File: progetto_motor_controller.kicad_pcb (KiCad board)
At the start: 4 copper layers, 66 x 75 mm, 114 parts, among them J1 USB_B_Micro, J2 Conn_01x06, J3 Conn_01x04, J4 Screw_Terminal_01x03, J5 Conn_01x05, J6 Conn_02x10_Odd_Even, J7 Conn_01x02, J8 Screw_Terminal_01x02, J9 Conn_01x03, Q1 BSC022N04LSATMA1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

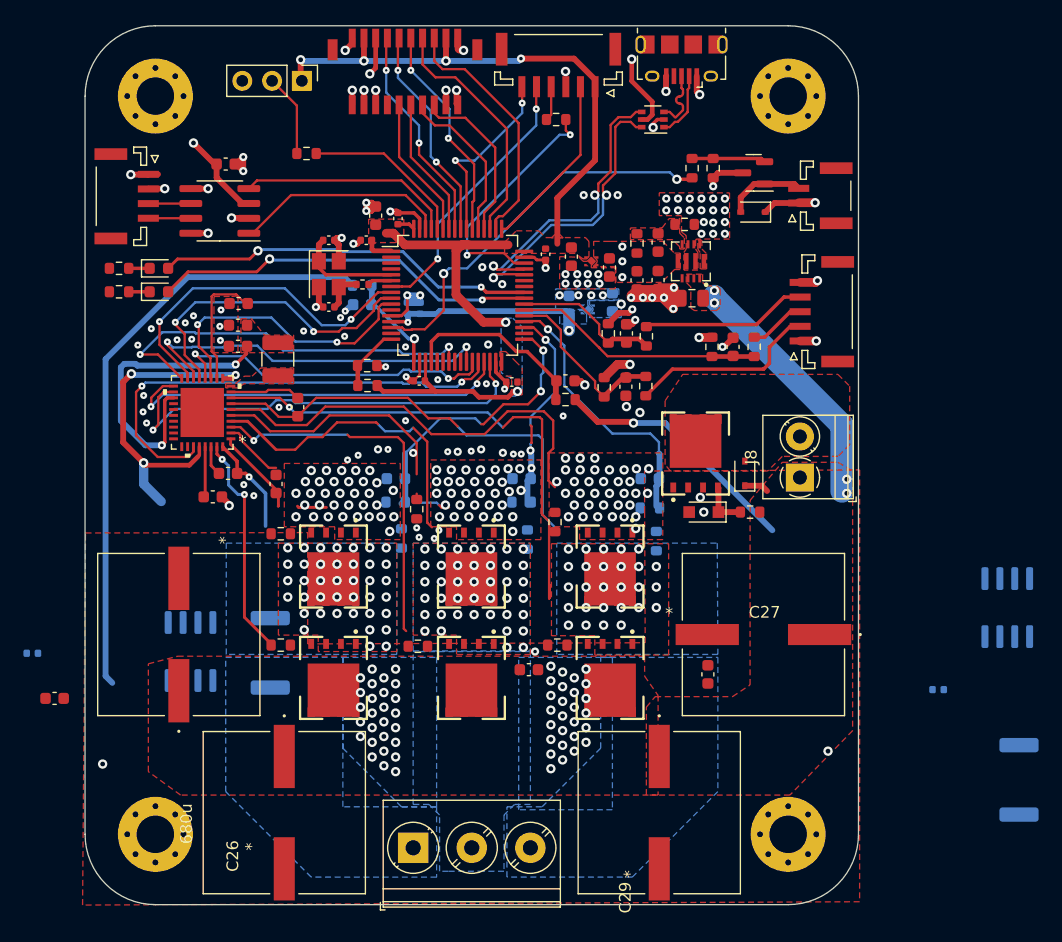
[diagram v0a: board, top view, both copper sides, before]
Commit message: added mosfet vias
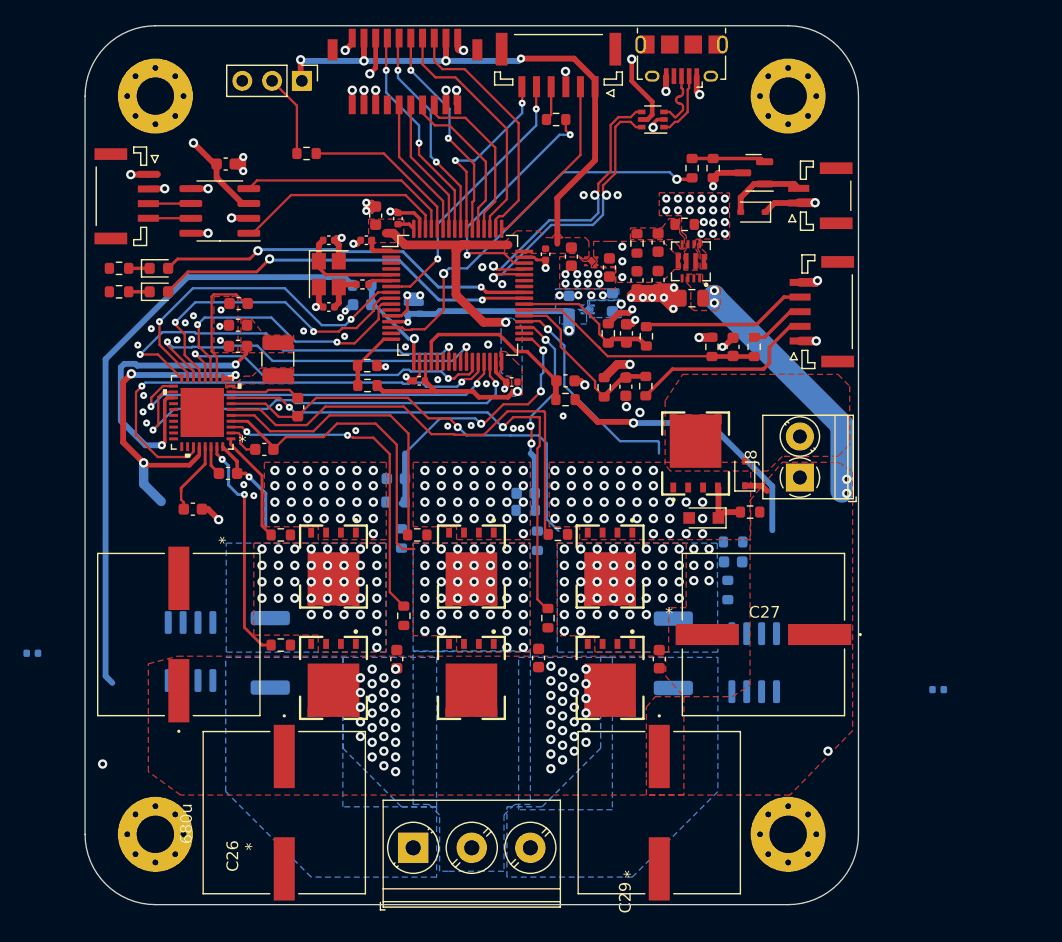
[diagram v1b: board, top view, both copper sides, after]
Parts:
- moved C20 41.4 mm to (121.7, 130.9), turned to 90 degrees
- moved R11 31.4 mm to (133.2, 130.6)
- moved U6 22.1 mm to (140.1, 131.3)
- moved C25 11.3 mm to (109.6, 131.1), turned to 90 degrees
- moved C22 10.0 mm to (138.3, 122.8), turned to 0 degrees
- moved R22 7.67 mm to (138.3, 121.0), turned to 0 degrees
- moved R19 7.39 mm to (137.8, 125.2)
- moved C23 4.35 mm to (132.0, 131.1)
- moved C14 3.11 mm to (98.3, 113.2), turned to 180 degrees
- moved R24 2.86 mm to (110.2, 127.3), turned to 90 degrees
- moved R16 2.44 mm to (122.5, 127.5), turned to 90 degrees
- moved R25 2.20 mm to (111.3, 120.5), turned to 180 degrees
- moved C12 2.00 mm to (92.2, 118.2)
- moved C21 1.30 mm to (120.6, 116.9)
- moved R17 1.08 mm to (123.3, 120.4), turned to 180 degrees
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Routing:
- net /Inverter/LB_G: track 24.2 -> 0.00 mm, vias 2 -> 0
- net /Inverter/LA_G: track 20.5 -> 0.00 mm
- net HA: track 24.3 -> 44.1 mm
- net HB: track 10.7 -> 28.0 mm
- net V_EMF_SENSE_A: track 23.4 -> 18.8 mm
- net LB: track 21.4 -> 25.6 mm, vias 1 -> 0
- net LA: track 36.9 -> 40.4 mm
- net /Inverter/CV: track 5.33 -> 3.11 mm
- net /Inverter/C2_OUT: track 21.4 -> 23.6 mm
- net LC: track 7.45 -> 9.59 mm
- net /Inverter/V10: track 4.33 -> 6.27 mm
- net GND: track 81.5 -> 79.8 mm, vias 211 -> 205
- net Net-(D6-Pad1): track 3.99 -> 4.70 mm
- net PH_B: vias 42 -> 41
- net PH_A_CS: vias 28 -> 41

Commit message: changed gate tracks layout
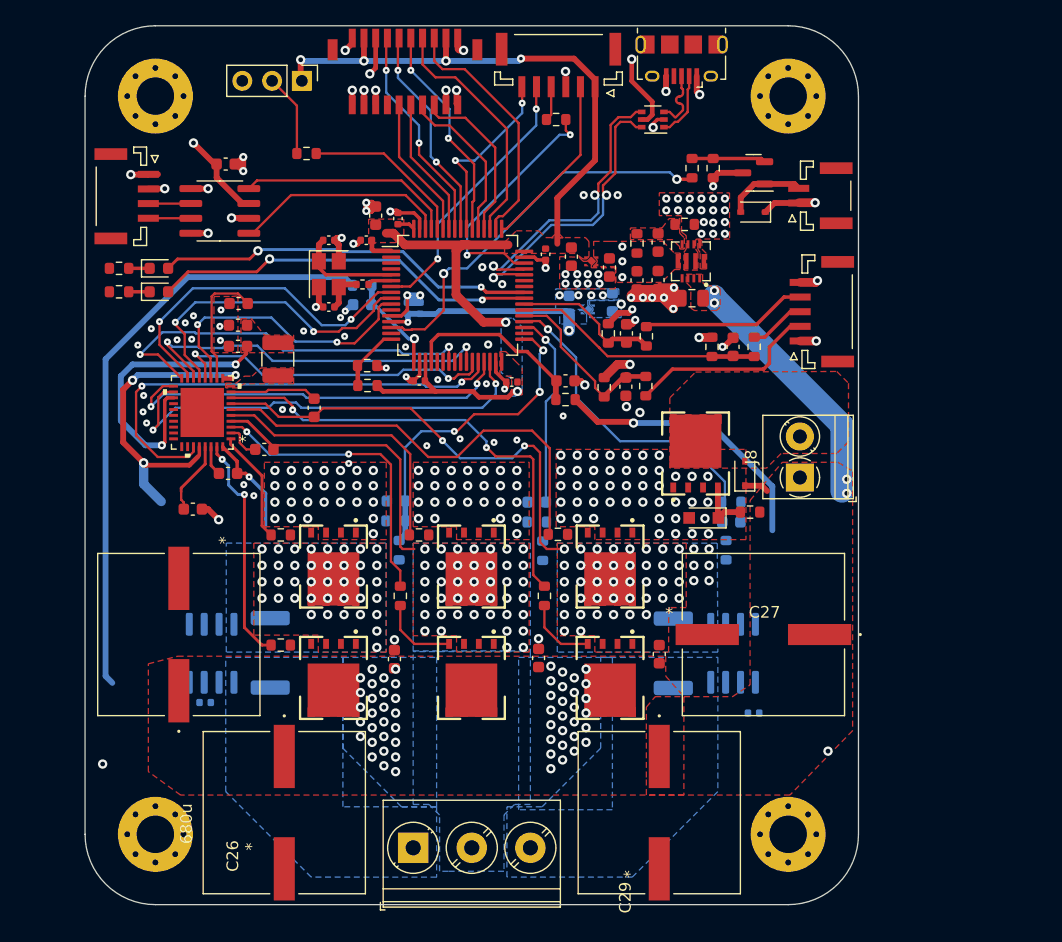
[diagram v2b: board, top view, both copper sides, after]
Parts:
- moved C16 15.9 mm to (140.1, 135.7)
- moved C17 15.3 mm to (93.2, 134.8)
- moved C22 3.40 mm to (138.2, 119.3)
- moved R19 3.40 mm to (137.7, 121.8)
- moved R22 3.40 mm to (138.2, 117.7)
- moved U6 1.97 mm to (138.3, 130.6)
- moved R16 1.92 mm to (122.2, 125.7)
- moved C24 1.90 mm to (109.5, 117.5)
- moved U5 1.81 mm to (93.8, 130.6)
- moved R24 1.73 mm to (109.9, 125.7)
- moved R23 1.60 mm to (109.5, 119.2)
- moved C13 1.40 mm to (102.5, 109.6)
- moved R21 1.38 mm to (121.5, 119.3)
- moved C21 1.21 mm to (121.5, 117.7)
- moved R20 1.02 mm to (109.8, 121.8)
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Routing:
- net V_EMF_SENSE_A: track 18.8 -> 26.7 mm
- net /Inverter/HB_G: track 0.00 -> 6.74 mm
- net /Inverter/HA_G: track 0.00 -> 6.15 mm
- net HA: track 44.1 -> 39.7 mm
- net V_EMF_SENSE_C: track 24.2 -> 27.4 mm
- net LA: track 40.4 -> 37.9 mm
- net HB: track 28.0 -> 25.7 mm
- net PH_B: track 27.1 -> 25.0 mm
- net PH_A_CS: track 37.6 -> 39.6 mm, vias 41 -> 42
- net LB: track 25.6 -> 23.6 mm
- net V_EMF_SENSE_B: track 18.3 -> 16.8 mm, vias 3 -> 1
- net /Inverter/CU: track 6.09 -> 7.51 mm
- net 3V3_TMC: track 25.3 -> 24.8 mm
- net GND: track 79.8 -> 79.9 mm, vias 205 -> 208

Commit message: layout
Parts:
- added R35: 3k9, Resistor_SMD:R_0603_1608Metric, B.Cu at (121.7, 118.2)
- added R36: 3k9, Resistor_SMD:R_0603_1608Metric, B.Cu at (109.5, 118.2)
- added R6: 3k9, Resistor_SMD:R_0603_1608Metric, B.Cu at (138.4, 118.2)
- moved C22 2.81 mm to (138.4, 116.5), turned to 180 degrees
- moved R22 2.31 mm to (138.4, 120.0)
- moved C12 1.75 mm to (92.6, 116.5), turned to -90 degrees
- moved C16 1.57 mm to (138.6, 135.1)
- moved C21 1.26 mm to (121.7, 116.4)
- moved C24 1.15 mm to (109.5, 116.4)
- moved R20 0.90 mm to (109.8, 122.7)
- moved R18 0.86 mm to (122.2, 122.7)
- moved R28 0.65 mm to (139.4, 119.0)
- moved R23 0.65 mm to (109.5, 119.9)
- moved R21 0.57 mm to (121.7, 119.9)
- moved C17 0.49 mm to (93.7, 134.9)
- moved C25 0.45 mm to (109.8, 131.1)
- moved R19 0.32 mm to (137.4, 121.7), turned to 0 degrees
- moved D5 0.18 mm to (139.4, 115.0)
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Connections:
- R18 pad 2: V_EMF_SENSE_B -> /Inverter/V_EMF_SENSE_B_NF
- R19 pad 2: V_EMF_SENSE_A -> /Inverter/V_EMF_SENSE_A_NF
- R20 pad 2: V_EMF_SENSE_C -> /Inverter/V_EMF_SENSE_C_NF
- R21 pad 1: V_EMF_SENSE_B -> /Inverter/V_EMF_SENSE_B_NF
- R22 pad 1: V_EMF_SENSE_A -> /Inverter/V_EMF_SENSE_A_NF
- R23 pad 1: V_EMF_SENSE_C -> /Inverter/V_EMF_SENSE_C_NF
- U4 pad 37: (no net) -> GND
- U7 pad : (no net) -> GND
- U7 pad 3: unconnected-(U7-Pad3) -> GND
- U7 pad 7: unconnected-(U7-Pad7) -> VDD
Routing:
- net 3V3_VDAA: track 53.2 -> 71.3 mm, vias 4 -> 6
- net VDD: track 51.1 -> 66.8 mm, vias 61 -> 75
- net /Inverter/C1_OUT: track 52.1 -> 66.3 mm
- net PH_C_CS: track 8.72 -> 22.2 mm
- net /Inverter/C2_OUT: track 23.6 -> 37.1 mm
- net PH_C: track 0.00 -> 9.53 mm
- net PH_A_CS: track 39.6 -> 47.5 mm
- net PH_A: track 0.00 -> 6.19 mm
- net GND: track 79.9 -> 85.7 mm, vias 208 -> 267
- net /Inverter/V_EMF_SENSE_B_NF: track 0.00 -> 3.83 mm
- net /Inverter/V_EMF_SENSE_C_NF: track 0.00 -> 3.82 mm
- net /Inverter/V_EMF_SENSE_A_NF: track 0.00 -> 3.67 mm
- net /Inverter/V10: track 6.27 -> 3.13 mm
- net V_EMF_SENSE_C: track 27.4 -> 24.8 mm
- net PH_B: track 25.0 -> 26.9 mm
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- added copper zone on In1.Cu, net VDD

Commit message: before load switch
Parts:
- added D3: D_Zener_Small, Diode_SMD:D_SOD-123, B.Cu at (134.9, 114.0)
- added D7: D_Zener_Small, Diode_SMD:D_SOD-123, B.Cu at (120.8, 114.2)
- added D8: D_Zener_Small, Diode_SMD:D_SOD-123, B.Cu at (108.6, 114.2)
- added D9: DESD32VS2SO, Package_TO_SOT_SMD:SOT-23, F.Cu at (92.2, 92.8)
- added U10: 74LVC3G17, Package_SO:VSSOP-8_2.3x2mm_P0.5mm, F.Cu at (124.8, 103.2)
- moved U2 3.70 mm to (98.2, 92.8)
- moved R1 3.27 mm to (100.0, 85.2)
- moved D4 3.11 mm to (140.3, 89.8)
- moved C8 3.10 mm to (98.1, 89.0)
- moved Q1 3.06 mm to (138.6, 86.8)
- moved R8 1.48 mm to (135.8, 87.9)
- moved R7 1.27 mm to (134.2, 88.0)
- moved J9 1.05 mm to (100.5, 81.7)
- moved R34 0.50 mm to (131.4, 103.5)
- moved C41 0.36 mm to (129.5, 103.5)
- moved J1 0.35 mm to (133.9, 79.5)
- moved R12 0.25 mm to (124.0, 109.2)
- moved R32 0.25 mm to (131.1, 107.8)
- moved R29 0.21 mm to (127.6, 103.5)
- moved R30 0.20 mm to (136.3, 104.4)
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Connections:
- C39 pad 1: ENC_A -> ENC_A_5V
- C40 pad 1: ENC_B -> ENC_B_5V
- C41 pad 1: ENC_I -> ENC_I_5V
- R29 pad 1: ENC_I -> ENC_I_5V
- R30 pad 1: ENC_B -> ENC_B_5V
- R31 pad 1: ENC_A -> ENC_A_5V
- R32 pad 1: ENC_A -> ENC_A_5V
- R33 pad 1: ENC_B -> ENC_B_5V
- R34 pad 1: ENC_I -> ENC_I_5V
- U1 pad 37: ENC_A -> ENC_B
- U1 pad 38: ENC_B -> ENC_I
- U1 pad 39: ENC_I -> ENC_A
- U4 pad 37: GND -> (no net)
- U7 pad : GND -> (no net)
- U7 pad 3: GND -> unconnected-(U7-Pad3)
- U7 pad 7: VDD -> unconnected-(U7-Pad7)
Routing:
- net ENC_B_5V: track 0.00 -> 16.1 mm
- net ENC_B: track 21.3 -> 5.68 mm
- net 3V3_MCU: track 87.1 -> 100.5 mm
- net ENC_I_5V: track 0.00 -> 10.3 mm
- net ENC_A_5V: track 0.00 -> 10.3 mm
- net ENC_A: track 15.3 -> 5.39 mm
- net ENC_I: track 12.7 -> 6.64 mm
- net VDD: track 66.8 -> 71.4 mm
- net 5V: track 32.5 -> 36.6 mm
- net CAN_L: track 3.63 -> 7.59 mm
- net CAN_H: track 3.63 -> 7.59 mm
- net CAN_TX: track 18.3 -> 14.6 mm
- net CAN_RX: track 18.5 -> 14.8 mm
- net GND: track 85.7 -> 89.1 mm, vias 267 -> 276
- net BOOT0: track 14.1 -> 17.1 mm
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- removed copper zone on B.Cu, net 3V3_MCU

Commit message: buck relayout
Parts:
- moved R26 7.37 mm to (137.2, 93.5), turned to 0 degrees
- moved C34 6.54 mm to (134.0, 93.5), turned to 180 degrees
- moved R27 5.88 mm to (138.8, 97.6), turned to -90 degrees
- moved C33 5.35 mm to (137.2, 95.3), turned to 0 degrees
- moved C35 4.02 mm to (134.1, 95.3), turned to 180 degrees
- moved C30 3.08 mm to (132.5, 98.2), turned to 90 degrees
- moved R8 1.95 mm to (136.8, 89.6), turned to 180 degrees
- moved R7 1.75 mm to (135.7, 87.0)
- moved U7 1.38 mm to (135.7, 98.1), turned to 90 degrees
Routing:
- net 5V: track 36.6 -> 41.6 mm, vias 15 -> 10
- net Net-(Q1-Pad2): track 6.23 -> 8.09 mm
- net GND: track 89.1 -> 87.3 mm, vias 276 -> 278
- net FAN_PWM: track 33.0 -> 34.8 mm

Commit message: final
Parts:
- removed D5: D_TVS, Diode_SMD:D_SOD-323
- added C44: 220n, Capacitor_SMD:C_0603_1608Metric, F.Cu at (90.7, 115.9)
- added C45: 220n, Capacitor_SMD:C_0603_1608Metric, B.Cu at (96.8, 107.0)
- added C49: 1n, Capacitor_SMD:C_0603_1608Metric, B.Cu at (96.7, 125.2)
- added C50: 1n, Capacitor_SMD:C_0603_1608Metric, B.Cu at (123.2, 125.2)
- added C51: 1n, Capacitor_SMD:C_0603_1608Metric, B.Cu at (110.8, 125.2)
- added Q9: AO3407A, Package_TO_SOT_SMD:SOT-23, F.Cu at (129.7, 89.0)
- added R37: 5.6k, Resistor_SMD:R_0603_1608Metric, B.Cu at (130.3, 94.3)
- added R38: 22k, Resistor_SMD:R_0603_1608Metric, B.Cu at (127.1, 94.3)
- added R39: 120, Resistor_SMD:R_1210_3225Metric, F.Cu at (95.4, 92.3)
- added TP1: Testpoint, MyLibrary:TestPoint_1.0mm, F.Cu at (92.5, 95.0)
- added TP11: TestPoint, MyLibrary:TestPoint_1.0mm, B.Cu at (122.7, 103.0)
- added TP12: TestPoint, MyLibrary:TestPoint_1.0mm, B.Cu at (123.8, 106.0)
- added TP13: TestPoint, MyLibrary:TestPoint_1.0mm, B.Cu at (121.0, 107.3)
- added TP14: TestPoint, MyLibrary:TestPoint_1.0mm, B.Cu at (127.3, 95.7)
- added TP15: TestPoint, MyLibrary:TestPoint_1.0mm, F.Cu at (139.2, 94.5)
- added TP16: TestPoint, MyLibrary:TestPoint_1.0mm, F.Cu at (137.8, 91.8)
- added TP17: TestPoint, MyLibrary:TestPoint_1.0mm, B.Cu at (122.1, 100.5)
- added TP18: TestPoint, MyLibrary:TestPoint_1.0mm, F.Cu at (123.2, 94.5)
- added TP19: TestPoint, MyLibrary:TestPoint_1.0mm, F.Cu at (111.7, 109.8)
- added TP2: TestPoint, MyLibrary:TestPoint_1.0mm, F.Cu at (98.6, 102.3)
- added TP20: Testpoint, MyLibrary:TestPoint_1.0mm, F.Cu at (88.2, 113.1)
- added TP21: Testpoint, MyLibrary:TestPoint_1.0mm, F.Cu at (88.9, 107.2)
- added TP22: Testpoint, MyLibrary:TestPoint_1.0mm, B.Cu at (118.4, 109.1)
- added TP23: Testpoint, MyLibrary:TestPoint_1.0mm, F.Cu at (106.3, 104.6)
- added TP24: Testpoint, MyLibrary:TestPoint_1.0mm, F.Cu at (103.1, 103.8)
- added TP25: Testpoint, MyLibrary:TestPoint_1.0mm, F.Cu at (106.3, 100.5)
- added TP26: Testpoint, MyLibrary:TestPoint_1.0mm, B.Cu at (114.7, 106.5)
- added TP27: Testpoint, MyLibrary:TestPoint_1.0mm, B.Cu at (116.2, 103.5)
- added TP3: TestPoint, MyLibrary:TestPoint_1.0mm, F.Cu at (123.5, 106.2)
- added TP30: Testpoint, MyLibrary:TestPoint_1.0mm, F.Cu at (92.5, 90.6)
- added TP31: Testpoint, MyLibrary:TestPoint_1.0mm, F.Cu at (132.8, 103.3)
- added TP32: Testpoint, MyLibrary:TestPoint_1.0mm, F.Cu at (132.4, 106.3)
- added TP33: Testpoint, MyLibrary:TestPoint_1.0mm, F.Cu at (134.3, 103.8)
- added TP4: TestPoint, MyLibrary:TestPoint_1.0mm, B.Cu at (108.5, 102.7)
- added TP5: TestPoint, MyLibrary:TestPoint_1.0mm, F.Cu at (97.5, 120.3)
- added TP6: TestPoint, MyLibrary:TestPoint_1.0mm, F.Cu at (96.5, 129.8)
- added TP7: TestPoint, MyLibrary:TestPoint_1.0mm, F.Cu at (122.3, 123.0)
- added TP8: TestPoint, MyLibrary:TestPoint_1.0mm, F.Cu at (122.3, 111.2)
- added TP9: TestPoint, MyLibrary:TestPoint_1.0mm, F.Cu at (109.8, 123.0)
- added U11: LM258, Package_SO:SOIC-8_3.9x4.9mm_P1.27mm, B.Cu at (129.7, 89.8)
- C11: footprint Capacitor_SMD:C_0603_1608Metric -> Capacitor_SMD:C_0402_1005Metric
- C13, C14, C15: value 680n -> 1u
- C16, C17: value 0.1uF -> 100n
- C20, C23, C25: footprint Capacitor_SMD:C_0603_1608Metric -> Capacitor_SMD:C_1206_3216Metric
- C30: footprint Capacitor_SMD:C_0805_2012Metric -> Capacitor_SMD:C_1206_3216Metric
- C42: footprint Capacitor_SMD:C_0402_1005Metric -> Capacitor_SMD:C_0603_1608Metric
- Q1: value BSC022N04LSATMA1 -> DMG3402L-7
- Q8: value BSC022N04LSATMA1 -> BSC010N04LSATMA1
- R14, R15, R16, R17, R24, R25: value 10 -> 2.2
- U3: footprint Package_TO_SOT_SMD:SOT-363_SC-70-6 -> Package_TO_SOT_SMD:SOT-23-6
- moved NTC1 9.19 mm to (115.3, 111.8), turned to -90 degrees
- moved R9 8.78 mm to (113.6, 111.9), turned to 90 degrees
- moved U2 3.10 mm to (101.2, 91.9)
- moved C8 2.89 mm to (100.8, 88.0)
- moved R19 2.73 mm to (136.1, 124.0), turned to 90 degrees
- moved R1 2.19 mm to (97.9, 85.6), turned to 90 degrees
- moved R26 1.80 mm to (137.2, 95.3)
- moved C33 1.80 mm to (137.2, 93.5)
- moved C42 1.41 mm to (111.9, 101.0)
- moved R5 1.39 mm to (86.8, 98.8)
- moved D2 1.32 mm to (90.1, 98.8)
- moved R2 1.31 mm to (86.8, 100.8)
- moved D1 1.25 mm to (90.0, 100.8)
- moved C43 1.00 mm to (110.6, 101.0)
- moved R4 0.98 mm to (123.6, 85.9)
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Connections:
- J1 pad 1: 5V -> 5V_USB
- R19 pad 1: PH_A_CS -> PH_A
- R20 pad 1: PH_C_CS -> PH_C
- U1 pad 25: unconnected-(U1-Pad25) -> DRV_STRONG
- U3 pad 1: USB_CONN_D- -> USB_D-
- U3 pad 3: USB_CONN_D+ -> USB_CONN_D-
- U3 pad 4: USB_D+ -> USB_CONN_D+
- U3 pad 6: USB_D- -> USB_D+
- U4 pad 37: (no net) -> GND
- U7 pad : (no net) -> GND
- U7 pad 3: unconnected-(U7-Pad3) -> GND
- U7 pad 7: unconnected-(U7-Pad7) -> VDD
- U8 pad 5: (no net) -> GND
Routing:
- net DRV_STRONG: track 0.00 -> 50.6 mm, vias 0 -> 2
- net PH_C: track 9.53 -> 21.5 mm, vias 0 -> 13
- net 5V: track 41.6 -> 52.4 mm, vias 10 -> 20
- net 5V_USB: track 0.00 -> 10.8 mm
- net PH_A: track 6.19 -> 16.6 mm, vias 0 -> 13
- net BOARD_TEMP: track 5.52 -> 14.9 mm
- net VDD: track 71.5 -> 79.6 mm, vias 75 -> 80
- net /Power/Vusb_En: track 0.00 -> 5.53 mm, vias 0 -> 1
- net FAN_PWM: track 34.8 -> 40.3 mm
- net /Power/Vcomp+: track 0.00 -> 5.42 mm
- net CAN_L: track 7.59 -> 12.7 mm
- net CAN_H: track 7.59 -> 12.6 mm
- net CAN_TX: track 14.6 -> 11.3 mm
- net PWM_LB: track 32.0 -> 34.7 mm
- net CAN_RX: track 14.8 -> 12.3 mm
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- added copper zone on B.Cu, net /Power/UNUSED
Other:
- board text added: "+"
- board text added: "-"
- board text added: "A"
- board text added: "B"
- board text added: "BOOT"
- board text added: "C"
- board text added: "CAN"
- board text added: "COMM/IO"
- board text added: "DEBUG"
- board text added: "ENC/HALL"
- board text added: "FAN"
- board text added: "JLCJLCJLCJCL"
- board text added: "RUN"

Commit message: last commit
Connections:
- U9 pad 5: (no net) -> GND
